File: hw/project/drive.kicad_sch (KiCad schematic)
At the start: 45 parts, among them Q3 STL110N10F7, Q4 STL110N10F7, Q5 STL110N10F7, Q6 STL110N10F7, Q7 STL110N10F7, Q8 STL110N10F7

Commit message: somewhat organize main groups
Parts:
- renumbered R20 to R17, R21 to R18, R22 to R19, R26 to R20, R27 to R21, R28 to R22, R29 to R23, R30 to R24, R31 to R25, R32 to R26, R33 to R27, R34 to R28, R35 to R29, R36 to R30, R37 to R31, R38 to R32, R39 to R33, R40 to R34, R41 to R35, R42 to R36, R43 to R37
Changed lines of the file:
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@@
 		(in_pos_files yes)
 		(dnp no)
-		(property "Reference" "R22"
+		(property "Reference" "R19"
 			(at 175.514 36.068 90)
 			(show_name no)
@@
 			(project "esc"
 				(path "/86a17c4d-db96-42a1-af84-d43fe593f4e6/f702d253-729e-40c3-ac6b-420be83d0138"
-					(reference "R22")
+					(reference "R19")
 					(unit 1)
 				)
@@
 		(dnp no)
 		(fields_autoplaced yes)
-		(property "Reference" "R40"
+		(property "Reference" "R34"
 			(at 151.13 156.21 90)
 			(show_name no)
@@
 			(project "esc"
 				(path "/86a17c4d-db96-42a1-af84-d43fe593f4e6/f702d253-729e-40c3-ac6b-420be83d0138"
-					(reference "R40")
+					(reference "R34")
 					(unit 1)
 				)
@@
 		(in_pos_files yes)
 		(dnp no)
-		(property "Reference" "R21"
+		(property "Reference" "R18"
 			(at 106.934 36.068 90)
 			(show_name no)
@@
 			(project "esc"
 				(path "/86a17c4d-db96-42a1-af84-d43fe593f4e6/f702d253-729e-40c3-ac6b-420be83d0138"
-					(reference "R21")
+					(reference "R18")
 					(unit 1)
 				)
@@
 		(in_pos_files yes)
 		(dnp no)
-		(property "Reference" "R31"
+		(property "Reference" "R25"
 			(at 193.04 91.4399 0)
 			(show_name no)
@@
 			(project "esc"
 				(path "/86a17c4d-db96-42a1-af84-d43fe593f4e6/f702d253-729e-40c3-ac6b-420be83d0138"
-					(reference "R31")
+					(reference "R25")
 					(unit 1)
 				)
@@
 		(in_pos_files yes)
 		(dnp no)
-		(property "Reference" "R20"
+		(property "Reference" "R17"
 			(at 38.354 36.068 90)
 			(show_name no)
@@
 			(project "esc"
 				(path "/86a17c4d-db96-42a1-af84-d43fe593f4e6/f702d253-729e-40c3-ac6b-420be83d0138"
-					(reference "R20")
+					(reference "R17")
 					(unit 1)
 				)
@@
 		(in_pos_files yes)
 		(dnp no)
-		(property "Reference" "R34"
+		(property "Reference" "R28"
 			(at 129.794 116.078 90)
 			(show_name no)
@@
 			(project "esc"
 				(path "/86a17c4d-db96-42a1-af84-d43fe593f4e6/f702d253-729e-40c3-ac6b-420be83d0138"
-					(reference "R34")
+					(reference "R28")
 					(unit 1)
 				)
@@
 		(in_pos_files yes)
 		(dnp no)
-		(property "Reference" "R33"
+		(property "Reference" "R27"
 			(at 81.534 116.078 90)
 			(show_name no)
@@
 			(project "esc"
 				(path "/86a17c4d-db96-42a1-af84-d43fe593f4e6/f702d253-729e-40c3-ac6b-420be83d0138"
-					(reference "R33")
+					(reference "R27")
 					(unit 1)
 				)
@@
 		(dnp no)
 		(fields_autoplaced yes)
-		(property "Reference" "R36"
+		(property "Reference" "R30"
 			(at 34.29 156.21 90)
 			(show_name no)
@@
 			(project "esc"
 				(path "/86a17c4d-db96-42a1-af84-d43fe593f4e6/f702d253-729e-40c3-ac6b-420be83d0138"
-					(reference "R36")
+					(reference "R30")
 					(unit 1)
 				)
@@
 		(in_pos_files yes)
 		(dnp no)
-		(property "Reference" "R32"
+		(property "Reference" "R26"
 			(at 33.274 116.078 90)
 			(show_name no)
@@
 			(project "esc"
 				(path "/86a17c4d-db96-42a1-af84-d43fe593f4e6/f702d253-729e-40c3-ac6b-420be83d0138"
-					(reference "R32")
+					(reference "R26")
 					(unit 1)
 				)
@@
 		(in_pos_files yes)
 		(dnp no)
-		(property "Reference" "R30"
+		(property "Reference" "R24"
 			(at 124.46 91.4399 0)
 			(show_name no)
@@
 			(project "esc"
 				(path "/86a17c4d-db96-42a1-af84-d43fe593f4e6/f702d253-729e-40c3-ac6b-420be83d0138"
-					(reference "R30")
+					(reference "R24")
 					(unit 1)
 				)
@@
 		(dnp no)
 		(fields_autoplaced yes)
-		(property "Reference" "R42"
+		(property "Reference" "R36"
 			(at 99.06 165.0999 0)
 			(show_name no)
@@
 			(project "esc"
 				(path "/86a17c4d-db96-42a1-af84-d43fe593f4e6/f702d253-729e-40c3-ac6b-420be83d0138"
-					(reference "R42")
+					(reference "R36")
 					(unit 1)
 				)
@@
 		(dnp no)
 		(fields_autoplaced yes)
-		(property "Reference" "R39"
+		(property "Reference" "R33"
 			(at 146.05 156.21 90)
 			(show_name no)
@@
 			(project "esc"
 				(path "/86a17c4d-db96-42a1-af84-d43fe593f4e6/f702d253-729e-40c3-ac6b-420be83d0138"
-					(reference "R39")
+					(reference "R33")
 					(unit 1)
 				)
@@
 		(in_pos_files yes)
 		(dnp no)
-		(property "Reference" "R26"
+		(property "Reference" "R20"
 			(at 38.354 74.168 90)
 			(show_name no)
@@
 			(project "esc"
 				(path "/86a17c4d-db96-42a1-af84-d43fe593f4e6/f702d253-729e-40c3-ac6b-420be83d0138"
-					(reference "R26")
+					(reference "R20")
 					(unit 1)
 				)
@@
 		(in_pos_files yes)
 		(dnp no)
-		(property "Reference" "R28"
+		(property "Reference" "R22"
 			(at 175.514 74.168 90)
 			(show_name no)
@@
 			(project "esc"
 				(path "/86a17c4d-db96-42a1-af84-d43fe593f4e6/f702d253-729e-40c3-ac6b-420be83d0138"
-					(reference "R28")
+					(reference "R22")
 					(unit 1)
 				)
@@
 		(dnp no)
 		(fields_autoplaced yes)
-		(property "Reference" "R38"
+		(property "Reference" "R32"
 			(at 92.71 156.21 90)
 			(show_name no)
@@
 			(project "esc"
 				(path "/86a17c4d-db96-42a1-af84-d43fe593f4e6/f702d253-729e-40c3-ac6b-420be83d0138"
-					(reference "R38")
+					(reference "R32")
 					(unit 1)
 				)
@@
 		(dnp no)
 		(fields_autoplaced yes)
-		(property "Reference" "R37"
+		(property "Reference" "R31"
 			(at 87.63 156.21 90)
 			(show_name no)
@@
 			(project "esc"
 				(path "/86a17c4d-db96-42a1-af84-d43fe593f4e6/f702d253-729e-40c3-ac6b-420be83d0138"
-					(reference "R37")
+					(reference "R31")
 					(unit 1)
 				)
@@
 		(in_pos_files yes)
 		(dnp no)
-		(property "Reference" "R27"
+		(property "Reference" "R21"
 			(at 106.934 74.168 90)
 			(show_name no)
@@
 			(project "esc"
 				(path "/86a17c4d-db96-42a1-af84-d43fe593f4e6/f702d253-729e-40c3-ac6b-420be83d0138"
-					(reference "R27")
+					(reference "R21")
 					(unit 1)
 				)
@@
 		(dnp no)
 		(fields_autoplaced yes)
-		(property "Reference" "R43"
+		(property "Reference" "R37"
 			(at 157.48 165.0999 0)
 			(show_name no)
@@
 			(project "esc"
 				(path "/86a17c4d-db96-42a1-af84-d43fe593f4e6/f702d253-729e-40c3-ac6b-420be83d0138"
-					(reference "R43")
+					(reference "R37")
 					(unit 1)
 				)
@@
 		(in_pos_files yes)
 		(dnp no)
-		(property "Reference" "R29"
+		(property "Reference" "R23"
 			(at 55.88 91.4399 0)
 			(show_name no)
@@
 			(project "esc"
 				(path "/86a17c4d-db96-42a1-af84-d43fe593f4e6/f702d253-729e-40c3-ac6b-420be83d0138"
-					(reference "R29")
+					(reference "R23")
 					(unit 1)
 				)
@@
 		(dnp no)
 		(fields_autoplaced yes)
-		(property "Reference" "R41"
+		(property "Reference" "R35"
 			(at 40.64 165.0999 0)
 			(show_name no)
@@
 			(project "esc"
 				(path "/86a17c4d-db96-42a1-af84-d43fe593f4e6/f702d253-729e-40c3-ac6b-420be83d0138"
-					(reference "R41")
+					(reference "R35")
 					(unit 1)
 				)
@@
 		(dnp no)
 		(fields_autoplaced yes)
-		(property "Reference" "R35"
+		(property "Reference" "R29"
 			(at 29.21 156.21 90)
 			(show_name no)
@@
 			(project "esc"
 				(path "/86a17c4d-db96-42a1-af84-d43fe593f4e6/f702d253-729e-40c3-ac6b-420be83d0138"
-					(reference "R35")
+					(reference "R29")
 					(unit 1)
 				)

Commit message: Place critical components near MCU
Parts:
- renumbered R17 to R16, R18 to R17, R19 to R18, R20 to R19, R21 to R20, R22 to R21, R23 to R22, R24 to R23, R25 to R24, R26 to R25, R27 to R26, R28 to R27, R29 to R28, R30 to R29, R31 to R30, R32 to R31, R33 to R32, R34 to R33, R35 to R34, R36 to R35, R37 to R36
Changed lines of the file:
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@@
 		(in_pos_files yes)
 		(dnp no)
-		(property "Reference" "R19"
+		(property "Reference" "R18"
 			(at 175.514 36.068 90)
 			(show_name no)
@@
 			(project "esc"
 				(path "/86a17c4d-db96-42a1-af84-d43fe593f4e6/f702d253-729e-40c3-ac6b-420be83d0138"
-					(reference "R19")
+					(reference "R18")
 					(unit 1)
 				)
@@
 		(dnp no)
 		(fields_autoplaced yes)
-		(property "Reference" "R34"
+		(property "Reference" "R33"
 			(at 151.13 156.21 90)
 			(show_name no)
@@
 			(project "esc"
 				(path "/86a17c4d-db96-42a1-af84-d43fe593f4e6/f702d253-729e-40c3-ac6b-420be83d0138"
-					(reference "R34")
+					(reference "R33")
 					(unit 1)
 				)
@@
 		(in_pos_files yes)
 		(dnp no)
-		(property "Reference" "R18"
+		(property "Reference" "R17"
 			(at 106.934 36.068 90)
 			(show_name no)
@@
 			(project "esc"
 				(path "/86a17c4d-db96-42a1-af84-d43fe593f4e6/f702d253-729e-40c3-ac6b-420be83d0138"
-					(reference "R18")
+					(reference "R17")
 					(unit 1)
 				)
@@
 		(in_pos_files yes)
 		(dnp no)
-		(property "Reference" "R25"
+		(property "Reference" "R24"
 			(at 193.04 91.4399 0)
 			(show_name no)
@@
 			(project "esc"
 				(path "/86a17c4d-db96-42a1-af84-d43fe593f4e6/f702d253-729e-40c3-ac6b-420be83d0138"
-					(reference "R25")
+					(reference "R24")
 					(unit 1)
 				)
@@
 		(in_pos_files yes)
 		(dnp no)
-		(property "Reference" "R17"
+		(property "Reference" "R16"
 			(at 38.354 36.068 90)
 			(show_name no)
@@
 			(project "esc"
 				(path "/86a17c4d-db96-42a1-af84-d43fe593f4e6/f702d253-729e-40c3-ac6b-420be83d0138"
-					(reference "R17")
+					(reference "R16")
 					(unit 1)
 				)
@@
 		(in_pos_files yes)
 		(dnp no)
-		(property "Reference" "R28"
+		(property "Reference" "R27"
 			(at 129.794 116.078 90)
 			(show_name no)
@@
 			(project "esc"
 				(path "/86a17c4d-db96-42a1-af84-d43fe593f4e6/f702d253-729e-40c3-ac6b-420be83d0138"
-					(reference "R28")
+					(reference "R27")
 					(unit 1)
 				)
@@
 		(in_pos_files yes)
 		(dnp no)
-		(property "Reference" "R27"
+		(property "Reference" "R26"
 			(at 81.534 116.078 90)
 			(show_name no)
@@
 			(project "esc"
 				(path "/86a17c4d-db96-42a1-af84-d43fe593f4e6/f702d253-729e-40c3-ac6b-420be83d0138"
-					(reference "R27")
+					(reference "R26")
 					(unit 1)
 				)
@@
 		(dnp no)
 		(fields_autoplaced yes)
-		(property "Reference" "R30"
+		(property "Reference" "R29"
 			(at 34.29 156.21 90)
 			(show_name no)
@@
 			(project "esc"
 				(path "/86a17c4d-db96-42a1-af84-d43fe593f4e6/f702d253-729e-40c3-ac6b-420be83d0138"
-					(reference "R30")
+					(reference "R29")
 					(unit 1)
 				)
@@
 		(in_pos_files yes)
 		(dnp no)
-		(property "Reference" "R26"
+		(property "Reference" "R25"
 			(at 33.274 116.078 90)
 			(show_name no)
@@
 			(project "esc"
 				(path "/86a17c4d-db96-42a1-af84-d43fe593f4e6/f702d253-729e-40c3-ac6b-420be83d0138"
-					(reference "R26")
+					(reference "R25")
 					(unit 1)
 				)
@@
 		(in_pos_files yes)
 		(dnp no)
-		(property "Reference" "R24"
+		(property "Reference" "R23"
 			(at 124.46 91.4399 0)
 			(show_name no)
@@
 			(project "esc"
 				(path "/86a17c4d-db96-42a1-af84-d43fe593f4e6/f702d253-729e-40c3-ac6b-420be83d0138"
-					(reference "R24")
+					(reference "R23")
 					(unit 1)
 				)
@@
 		(dnp no)
 		(fields_autoplaced yes)
-		(property "Reference" "R36"
+		(property "Reference" "R35"
 			(at 99.06 165.0999 0)
 			(show_name no)
@@
 			(project "esc"
 				(path "/86a17c4d-db96-42a1-af84-d43fe593f4e6/f702d253-729e-40c3-ac6b-420be83d0138"
-					(reference "R36")
+					(reference "R35")
 					(unit 1)
 				)
@@
 		(dnp no)
 		(fields_autoplaced yes)
-		(property "Reference" "R33"
+		(property "Reference" "R32"
 			(at 146.05 156.21 90)
 			(show_name no)
@@
 			(project "esc"
 				(path "/86a17c4d-db96-42a1-af84-d43fe593f4e6/f702d253-729e-40c3-ac6b-420be83d0138"
-					(reference "R33")
+					(reference "R32")
 					(unit 1)
 				)
@@
 		(in_pos_files yes)
 		(dnp no)
-		(property "Reference" "R20"
+		(property "Reference" "R19"
 			(at 38.354 74.168 90)
 			(show_name no)
@@
 			(project "esc"
 				(path "/86a17c4d-db96-42a1-af84-d43fe593f4e6/f702d253-729e-40c3-ac6b-420be83d0138"
-					(reference "R20")
+					(reference "R19")
 					(unit 1)
 				)
@@
 		(in_pos_files yes)
 		(dnp no)
-		(property "Reference" "R22"
+		(property "Reference" "R21"
 			(at 175.514 74.168 90)
 			(show_name no)
@@
 			(project "esc"
 				(path "/86a17c4d-db96-42a1-af84-d43fe593f4e6/f702d253-729e-40c3-ac6b-420be83d0138"
-					(reference "R22")
+					(reference "R21")
 					(unit 1)
 				)
@@
 		(dnp no)
 		(fields_autoplaced yes)
-		(property "Reference" "R32"
+		(property "Reference" "R31"
 			(at 92.71 156.21 90)
 			(show_name no)
@@
 			(project "esc"
 				(path "/86a17c4d-db96-42a1-af84-d43fe593f4e6/f702d253-729e-40c3-ac6b-420be83d0138"
-					(reference "R32")
+					(reference "R31")
 					(unit 1)
 				)
@@
 		(dnp no)
 		(fields_autoplaced yes)
-		(property "Reference" "R31"
+		(property "Reference" "R30"
 			(at 87.63 156.21 90)
 			(show_name no)
@@
 			(project "esc"
 				(path "/86a17c4d-db96-42a1-af84-d43fe593f4e6/f702d253-729e-40c3-ac6b-420be83d0138"
-					(reference "R31")
+					(reference "R30")
 					(unit 1)
 				)
@@
 		(in_pos_files yes)
 		(dnp no)
-		(property "Reference" "R21"
+		(property "Reference" "R20"
 			(at 106.934 74.168 90)
 			(show_name no)
@@
 			(project "esc"
 				(path "/86a17c4d-db96-42a1-af84-d43fe593f4e6/f702d253-729e-40c3-ac6b-420be83d0138"
-					(reference "R21")
+					(reference "R20")
 					(unit 1)
 				)
@@
 		(dnp no)
 		(fields_autoplaced yes)
-		(property "Reference" "R37"
+		(property "Reference" "R36"
 			(at 157.48 165.0999 0)
 			(show_name no)
@@
 			(project "esc"
 				(path "/86a17c4d-db96-42a1-af84-d43fe593f4e6/f702d253-729e-40c3-ac6b-420be83d0138"
-					(reference "R37")
+					(reference "R36")
 					(unit 1)
 				)
@@
 		(in_pos_files yes)
 		(dnp no)
-		(property "Reference" "R23"
+		(property "Reference" "R22"
 			(at 55.88 91.4399 0)
 			(show_name no)
@@
 			(project "esc"
 				(path "/86a17c4d-db96-42a1-af84-d43fe593f4e6/f702d253-729e-40c3-ac6b-420be83d0138"
-					(reference "R23")
+					(reference "R22")
 					(unit 1)
 				)
@@
 		(dnp no)
 		(fields_autoplaced yes)
-		(property "Reference" "R35"
+		(property "Reference" "R34"
 			(at 40.64 165.0999 0)
 			(show_name no)
@@
 			(project "esc"
 				(path "/86a17c4d-db96-42a1-af84-d43fe593f4e6/f702d253-729e-40c3-ac6b-420be83d0138"
-					(reference "R35")
+					(reference "R34")
 					(unit 1)
 				)
@@
 		(dnp no)
 		(fields_autoplaced yes)
-		(property "Reference" "R29"
+		(property "Reference" "R28"
 			(at 29.21 156.21 90)
 			(show_name no)
@@
 			(project "esc"
 				(path "/86a17c4d-db96-42a1-af84-d43fe593f4e6/f702d253-729e-40c3-ac6b-420be83d0138"
-					(reference "R29")
+					(reference "R28")
 					(unit 1)
 				)

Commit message: Update bulk caps
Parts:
- R22, R23, R24: JLCPCB (none) -> https://jlcpcb.com/partdetail/RESI-MCSM2512DL500K9/C53447178; LCSC (none) -> C53447178
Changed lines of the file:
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@@
 			)
 		)
+		(property "LCSC" "C53447178"
+			(at 195.58 92.71 0)
+			(hide yes)
+			(show_name no)
+			(do_not_autoplace no)
+			(effects
+				(font
+					(size 1.27 1.27)
+				)
+			)
+		)
+		(property "JLCPCB" "https://jlcpcb.com/partdetail/RESI-MCSM2512DL500K9/C53447178"
+			(at 195.58 92.71 0)
+			(hide yes)
+			(show_name no)
+			(do_not_autoplace no)
+			(effects
+				(font
+					(size 1.27 1.27)
+				)
+			)
+		)
 		(pin "2"
 		)
@@
 			)
 		)
+		(property "LCSC" "C53447178"
+			(at 127 92.71 0)
+			(hide yes)
+			(show_name no)
+			(do_not_autoplace no)
+			(effects
+				(font
+					(size 1.27 1.27)
+				)
+			)
+		)
+		(property "JLCPCB" "https://jlcpcb.com/partdetail/RESI-MCSM2512DL500K9/C53447178"
+			(at 127 92.71 0)
+			(hide yes)
+			(show_name no)
+			(do_not_autoplace no)
+			(effects
+				(font
+					(size 1.27 1.27)
+				)
+			)
+		)
 		(pin "1"
 		)
@@
 			(at 58.42 92.71 0)
 			(hide yes)
+			(show_name no)
+			(do_not_autoplace no)
+			(effects
+				(font
+					(size 1.27 1.27)
+				)
+			)
+		)
+		(property "LCSC" "C53447178"
+			(at 58.42 92.71 0)
+			(hide yes)
+			(show_name no)
+			(do_not_autoplace no)
+			(effects
+				(font
+					(size 1.27 1.27)
+				)
+			)
+		)
+		(property "JLCPCB" "https://jlcpcb.com/partdetail/RESI-MCSM2512DL500K9/C53447178"
+			(at 58.42 92.71 0)
+			(hide yes)

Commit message: Spec everything with LCSC except for simple passives and header pins
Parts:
- D10, D11, D6, D7, D8, D9: JLCPCB (none) -> https://jlcpcb.com/partdetail/STMicroelectronics-BAT48JFILM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; LCSC (none) -> C2798199
- Q3, Q4, Q5, Q6, Q7, Q8: JLCPCB (none) -> https://jlcpcb.com/partdetail/STMicroelectronics-STL110N10F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; LCSC (none) -> C672185

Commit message: Update all components to LCSC version/alternative!
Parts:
- C26, C27, C28: value 220nF/100V -> 0.22uF/100V; JLCPCB (none) -> https://jlcpcb.com/partdetail/TaiyoYuden-HMK107C7224KAHTE/C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; LCSC (none) -> C2169715
- C29, C30, C31: value 1uF/25V -> 1uF/50V; JLCPCB (none) -> https://jlcpcb.com/partdetail/16531-CL10A105KB8NNNC/C15849; LCSC (none) -> C15849
- C32, C33, C34: value 1nF -> 1nF/100V; JLCPCB (none) -> https://jlcpcb.com/partdetail/YAGEO-CC0603JRNPO0BN102/C1137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; LCSC (none) -> C113793
- C35, C36, C37: JLCPCB (none) -> https://jlcpcb.com/partdetail/YAGEO-CC0603JRNPO0BN471/C3269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; LCSC (none) -> C326973
- R16, R17, R18, R19, R20, R21, R25, R26, R27: JLCPCB (none) -> https://jlcpcb.com/partdetail/23586-0603WAF100JT5E/C22859; LCSC (none) -> C22859
- R28, R29, R30, R31, R32, R33: JLCPCB (none) -> https://jlcpcb.com/partdetail/26704-0603WAF2212T5E/C25961; LCSC (none) -> C25961
- R34, R35, R36: JLCPCB (none) -> https://jlcpcb.com/partdetail/4597-0603WAF2201T5E/C4190; LCSC (none) -> C4190

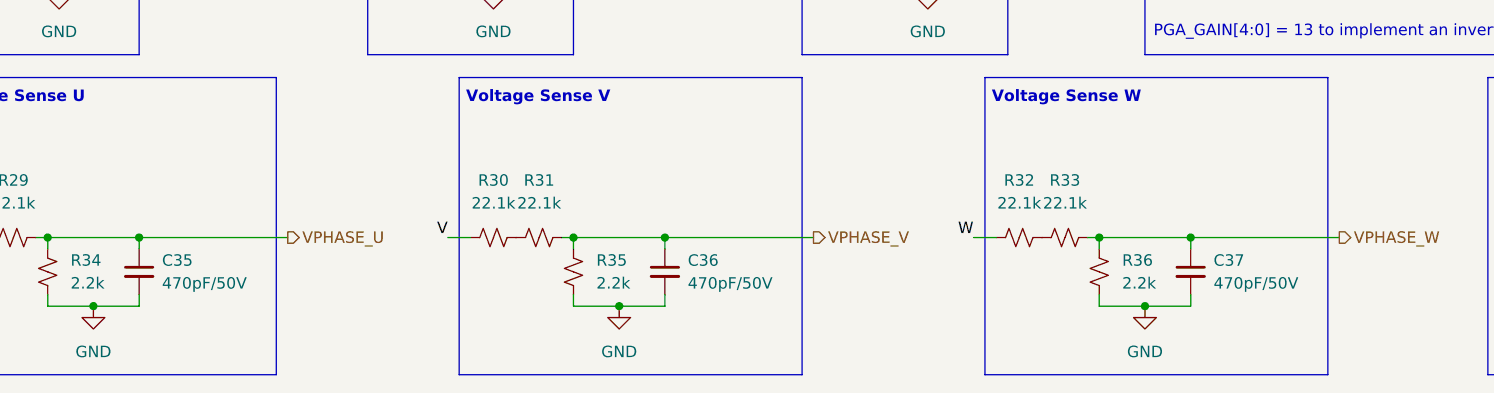
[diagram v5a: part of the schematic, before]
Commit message: Reclear ERC errors and resolve new PCB footprints after LCSC parts shift
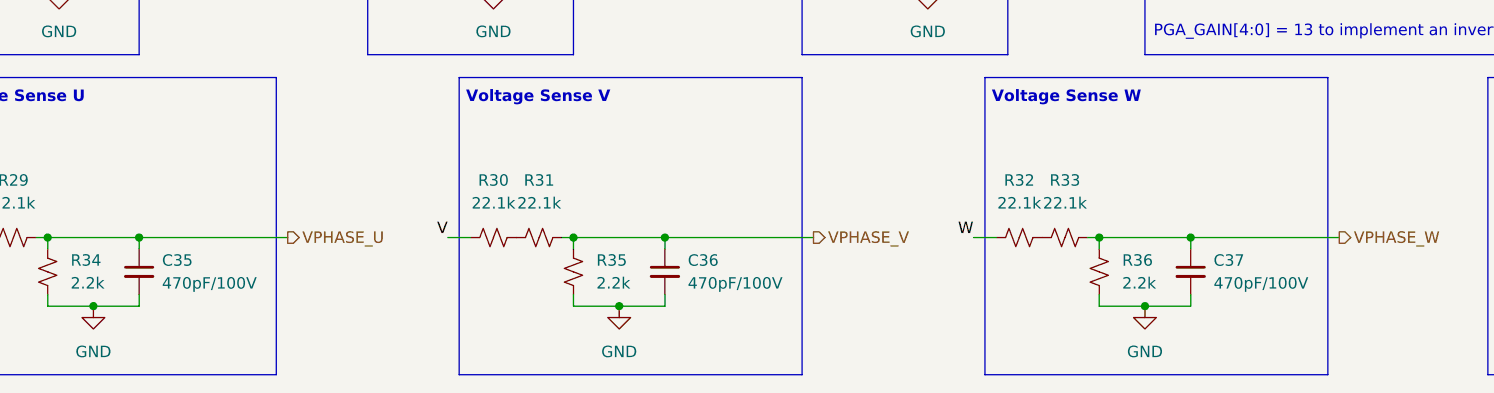
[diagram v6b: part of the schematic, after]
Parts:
- C35, C36, C37: value 470pF/50V -> 470pF/100V
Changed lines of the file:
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@@
 			)
 		)
-		(property "Value" "470pF/50V"
+		(property "Value" "470pF/100V"
 			(at 109.22 167.6462 0)
 			(show_name no)
@@
 			)
 		)
-		(property "Value" "470pF/50V"
+		(property "Value" "470pF/100V"
 			(at 167.64 167.6462 0)
 			(show_name no)
@@
 			)
 		)
-		(property "Value" "470pF/50V"
+		(property "Value" "470pF/100V"
 			(at 50.8 167.6462 0)
 			(show_name no)
